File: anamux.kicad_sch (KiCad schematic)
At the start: 3 parts, among them J51 Conn_02x08_Odd_Even, U26 CD4051B

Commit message: WIP v0.2.0 changes
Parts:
- J45: renamed from J51; value Conn_02x08_Odd_Even -> Conn_01x08; footprint HL_Connector_Pad_2.54mm:Pad_2x08_P2.54_1.7x1.7_Rect-Oct -> HL_Connector_Pad_2.54mm:Pad_1x08_P2.54_1.7x1.7_Oct; symbol Connector_Generic:Conn_02x08_Odd_Even -> Connector_Generic:Conn_01x08
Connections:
- net GND: no longer J45.1 (Pin_1), J45.11 (Pin_11), J45.13 (Pin_13), J45.15 (Pin_15), J45.3 (Pin_3), J45.5 (Pin_5), J45.7 (Pin_7), J45.9 (Pin_9)
- net X0: now also J45.1 (Pin_1); no longer J45.2 (Pin_2)
- net X1: now also J45.2 (Pin_2); no longer J45.4 (Pin_4)
- net X2: now also J45.3 (Pin_3); no longer J45.6 (Pin_6)
- net X3: now also J45.4 (Pin_4); no longer J45.8 (Pin_8)
- net X4: now also J45.5 (Pin_5); no longer J45.10 (Pin_10)
- net X5: now also J45.6 (Pin_6); no longer J45.12 (Pin_12)
- net X6: now also J45.7 (Pin_7); no longer J45.14 (Pin_14)
- net X7: now also J45.8 (Pin_8); no longer J45.16 (Pin_16)

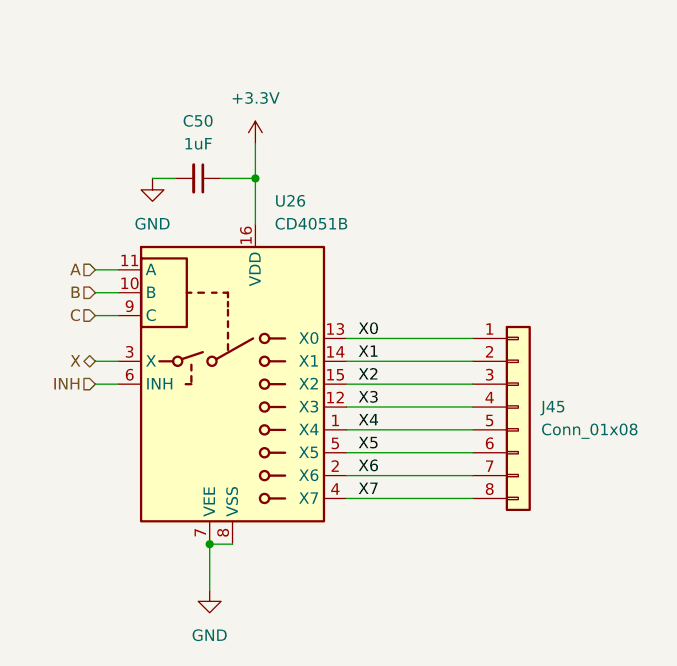
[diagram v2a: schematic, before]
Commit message: Assign part numbers and finish other 0.2.0 changes
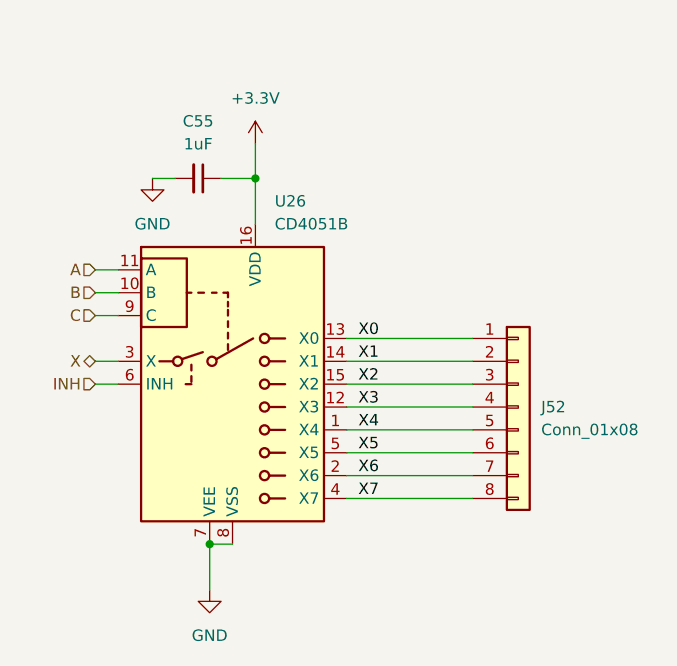
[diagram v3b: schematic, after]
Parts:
- J52: renamed from J45; LCSC (none) -> C492407
- renumbered C50 to C55
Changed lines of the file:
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@@
 		(dnp no)
 		(fields_autoplaced yes)
-		(property "Reference" "J45"
+		(property "Reference" "J52"
 			(at 123.19 78.7399 0)
 			(effects
@@
 					(size 1.27 1.27)
 				)
+			)
+		)
+		(property "LCSC" "C492407"
+			(at 120.65 78.74 0)
+			(effects
+				(font
+					(size 1.27 1.27)
+				)
+				(hide yes)
 			)
 		)
@@
 			(project ""
 				(path "/7eeba806-440e-4671-bc07-69fe183910a7/c1640104-e93c-4dad-89ee-86b02155c684/6bf2b6cc-eb81-4d9f-a81d-b7f6cfd4faa9"
-					(reference "J45")
+					(reference "J52")
 					(unit 1)
 				)
 				(path "/7eeba806-440e-4671-bc07-69fe183910a7/c1640104-e93c-4dad-89ee-86b02155c684/7f1d0812-6a9e-4744-8af9-695086760ff2"
-					(reference "J55")
+					(reference "J61")
 					(unit 1)
 				)
 				(path "/7eeba806-440e-4671-bc07-69fe183910a7/c1640104-e93c-4dad-89ee-86b02155c684/884a68a7-a98a-499d-b804-4c3e5a6711fb"
-					(reference "J49")
+					(reference "J56")
 					(unit 1)
 				)
 				(path "/7eeba806-440e-4671-bc07-69fe183910a7/c1640104-e93c-4dad-89ee-86b02155c684/93528cc8-9ea6-4e83-9001-dc55f14534f1"
-					(reference "J54")
+					(reference "J60")
 					(unit 1)
 				)
@@
 		(dnp no)
 		(fields_autoplaced yes)
-		(property "Reference" "#PWR0196"
+		(property "Reference" "#PWR0207"
 			(at 80.01 59.69 0)
 			(effects
@@
 			(project "HALSPA"
 				(path "/7eeba806-440e-4671-bc07-69fe183910a7/c1640104-e93c-4dad-89ee-86b02155c684/6bf2b6cc-eb81-4d9f-a81d-b7f6cfd4faa9"
-					(reference "#PWR0196")
+					(reference "#PWR0207")
 					(unit 1)
 				)
 				(path "/7eeba806-440e-4671-bc07-69fe183910a7/c1640104-e93c-4dad-89ee-86b02155c684/7f1d0812-6a9e-4744-8af9-695086760ff2"
-					(reference "#PWR0238")
+					(reference "#PWR0243")
 					(unit 1)
 				)
 				(path "/7eeba806-440e-4671-bc07-69fe183910a7/c1640104-e93c-4dad-89ee-86b02155c684/884a68a7-a98a-499d-b804-4c3e5a6711fb"
-					(reference "#PWR0214")
+					(reference "#PWR0223")
 					(unit 1)
 				)
 				(path "/7eeba806-440e-4671-bc07-69fe183910a7/c1640104-e93c-4dad-89ee-86b02155c684/93528cc8-9ea6-4e83-9001-dc55f14534f1"
-					(reference "#PWR0234")
+					(reference "#PWR0240")
 					(unit 1)
 				)
@@
 		(dnp no)
 		(fields_autoplaced yes)
-		(property "Reference" "#PWR0197"
+		(property "Reference" "#PWR0208"
 			(at 86.36 105.41 0)
 			(effects
@@
 			(project "HALSPA"
 				(path "/7eeba806-440e-4671-bc07-69fe183910a7/c1640104-e93c-4dad-89ee-86b02155c684/6bf2b6cc-eb81-4d9f-a81d-b7f6cfd4faa9"
-					(reference "#PWR0197")
+					(reference "#PWR0208")
 					(unit 1)
 				)
 				(path "/7eeba806-440e-4671-bc07-69fe183910a7/c1640104-e93c-4dad-89ee-86b02155c684/7f1d0812-6a9e-4744-8af9-695086760ff2"
-					(reference "#PWR0239")
+					(reference "#PWR0244")
 					(unit 1)
 				)
 				(path "/7eeba806-440e-4671-bc07-69fe183910a7/c1640104-e93c-4dad-89ee-86b02155c684/884a68a7-a98a-499d-b804-4c3e5a6711fb"
-					(reference "#PWR0215")
+					(reference "#PWR0224")
 					(unit 1)
 				)
 				(path "/7eeba806-440e-4671-bc07-69fe183910a7/c1640104-e93c-4dad-89ee-86b02155c684/93528cc8-9ea6-4e83-9001-dc55f14534f1"
-					(reference "#PWR0235")
+					(reference "#PWR0241")
 					(unit 1)
 				)
@@
 		(dnp no)
 		(fields_autoplaced yes)
-		(property "Reference" "C50"
+		(property "Reference" "C55"
 			(at 85.0836 46.99 90)
 			(effects
@@
 			(project "HALSPA"
 				(path "/7eeba806-440e-4671-bc07-69fe183910a7/c1640104-e93c-4dad-89ee-86b02155c684/6bf2b6cc-eb81-4d9f-a81d-b7f6cfd4faa9"
-					(reference "C50")
+					(reference "C55")
 					(unit 1)
 				)
 				(path "/7eeba806-440e-4671-bc07-69fe183910a7/c1640104-e93c-4dad-89ee-86b02155c684/7f1d0812-6a9e-4744-8af9-695086760ff2"
-					(reference "C60")
+					(reference "C65")
 					(unit 1)
 				)
 				(path "/7eeba806-440e-4671-bc07-69fe183910a7/c1640104-e93c-4dad-89ee-86b02155c684/884a68a7-a98a-499d-b804-4c3e5a6711fb"
-					(reference "C54")
+					(reference "C59")
 					(unit 1)
 				)
 				(path "/7eeba806-440e-4671-bc07-69fe183910a7/c1640104-e93c-4dad-89ee-86b02155c684/93528cc8-9ea6-4e83-9001-dc55f14534f1"
-					(reference "C59")
+					(reference "C64")
 					(unit 1)
 				)
@@
 		(dnp no)
 		(fields_autoplaced yes)
-		(property "Reference" "#PWR0198"
+		(property "Reference" "#PWR0209"
 			(at 91.44 53.34 0)
 			(effects
@@
 			(project "HALSPA"
 				(path "/7eeba806-440e-4671-bc07-69fe183910a7/c1640104-e93c-4dad-89ee-86b02155c684/6bf2b6cc-eb81-4d9f-a81d-b7f6cfd4faa9"
-					(reference "#PWR0198")
+					(reference "#PWR0209")
 					(unit 1)
 				)
 				(path "/7eeba806-440e-4671-bc07-69fe183910a7/c1640104-e93c-4dad-89ee-86b02155c684/7f1d0812-6a9e-4744-8af9-695086760ff2"
-					(reference "#PWR0240")
+					(reference "#PWR0245")
 					(unit 1)
 				)
 				(path "/7eeba806-440e-4671-bc07-69fe183910a7/c1640104-e93c-4dad-89ee-86b02155c684/884a68a7-a98a-499d-b804-4c3e5a6711fb"
-					(reference "#PWR0216")
+					(reference "#PWR0225")
 					(unit 1)
 				)
 				(path "/7eeba806-440e-4671-bc07-69fe183910a7/c1640104-e93c-4dad-89ee-86b02155c684/93528cc8-9ea6-4e83-9001-dc55f14534f1"
-					(reference "#PWR0236")
-					(unit 1)
-				)
+					(reference "#PWR0242")
+					(unit 1)
+				)

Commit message: Update the title blocks
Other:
- company: (none) -> Hat Labs Oy
- title: (none) -> HALSPA - Hat Labs Spaghetti Board
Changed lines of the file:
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@@
 	(generator_version "9.0")
 	(paper "A4")
+	(title_block
+		(title "HALSPA - Hat Labs Spaghetti Board")
+		(date "2025-04-17")
+		(rev "v0.2.0")
+		(company "Hat Labs Oy")
+		(comment 1 "See the accompanying LICENSE.md file for license details.")
+	)
 	(junction
 		(at 91.44 53.34)

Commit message: Fix minor production issues
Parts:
- J52: JLCPCB_CORRECTION (none) -> 0;8.89;270
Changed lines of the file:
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@@
+			)
+		)
+		(property "JLCPCB_CORRECTION" "0;8.89;270"
+			(at 120.65 78.74 0)
+			(effects
+				(font
+					(size 1.27 1.27)
+				)
 			)
 		)

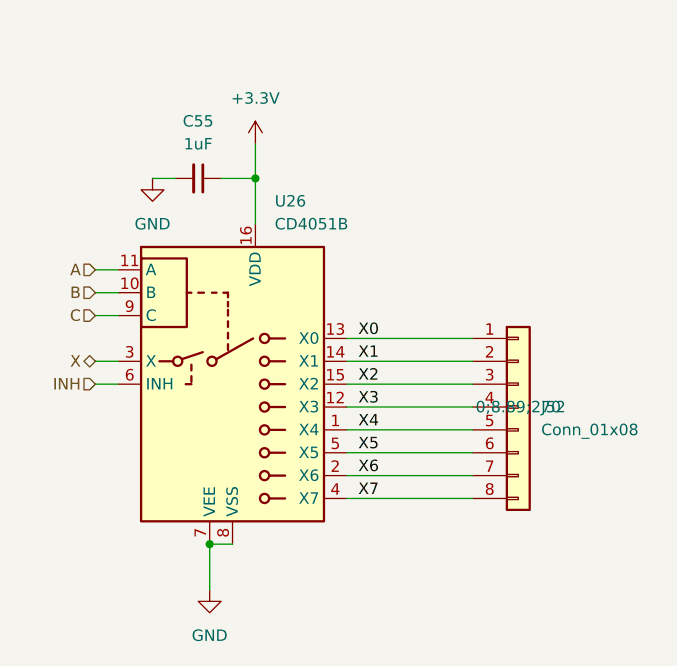
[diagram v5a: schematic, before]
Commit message: Improve MCU2 layout; document curlim12v CSA
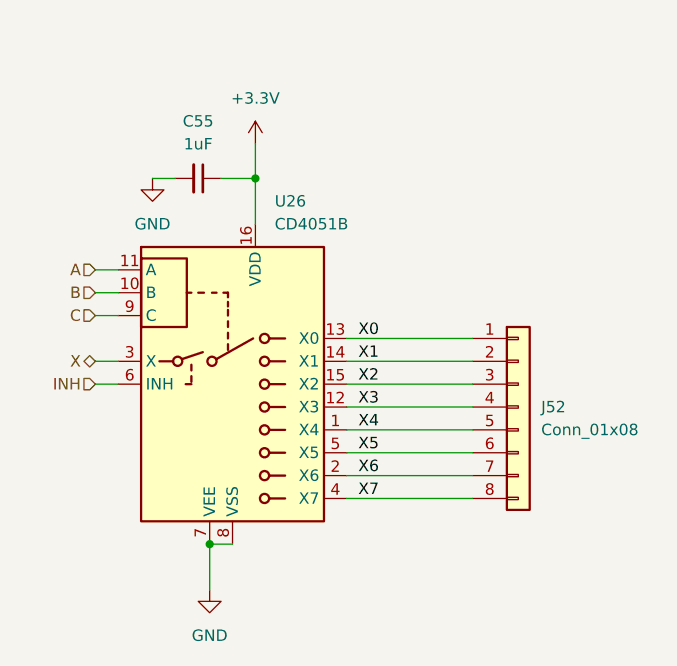
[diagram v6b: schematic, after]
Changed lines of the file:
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@@
 					(size 1.27 1.27)
 				)
+				(hide yes)
 			)
 		)
@@
 				)
 				(path "/7eeba806-440e-4671-bc07-69fe183910a7/c1640104-e93c-4dad-89ee-86b02155c684/7f1d0812-6a9e-4744-8af9-695086760ff2"
-					(reference "#PWR0243")
+					(reference "#PWR0244")
 					(unit 1)
 				)
@@
 				)
 				(path "/7eeba806-440e-4671-bc07-69fe183910a7/c1640104-e93c-4dad-89ee-86b02155c684/93528cc8-9ea6-4e83-9001-dc55f14534f1"
-					(reference "#PWR0240")
+					(reference "#PWR0241")
 					(unit 1)
 				)
@@
 				)
 				(path "/7eeba806-440e-4671-bc07-69fe183910a7/c1640104-e93c-4dad-89ee-86b02155c684/7f1d0812-6a9e-4744-8af9-695086760ff2"
-					(reference "#PWR0244")
+					(reference "#PWR0245")
 					(unit 1)
 				)
@@
 				)
 				(path "/7eeba806-440e-4671-bc07-69fe183910a7/c1640104-e93c-4dad-89ee-86b02155c684/93528cc8-9ea6-4e83-9001-dc55f14534f1"
-					(reference "#PWR0241")
+					(reference "#PWR0242")
 					(unit 1)
 				)
@@
 				)
 				(path "/7eeba806-440e-4671-bc07-69fe183910a7/c1640104-e93c-4dad-89ee-86b02155c684/7f1d0812-6a9e-4744-8af9-695086760ff2"
-					(reference "#PWR0245")
+					(reference "#PWR0246")
 					(unit 1)
 				)
@@
 				)
 				(path "/7eeba806-440e-4671-bc07-69fe183910a7/c1640104-e93c-4dad-89ee-86b02155c684/93528cc8-9ea6-4e83-9001-dc55f14534f1"
-					(reference "#PWR0242")
-					(unit 1)
-				)
+					(reference "#PWR0243")
+					(unit 1)
+				)

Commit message: Update anamux labeling and title blocks
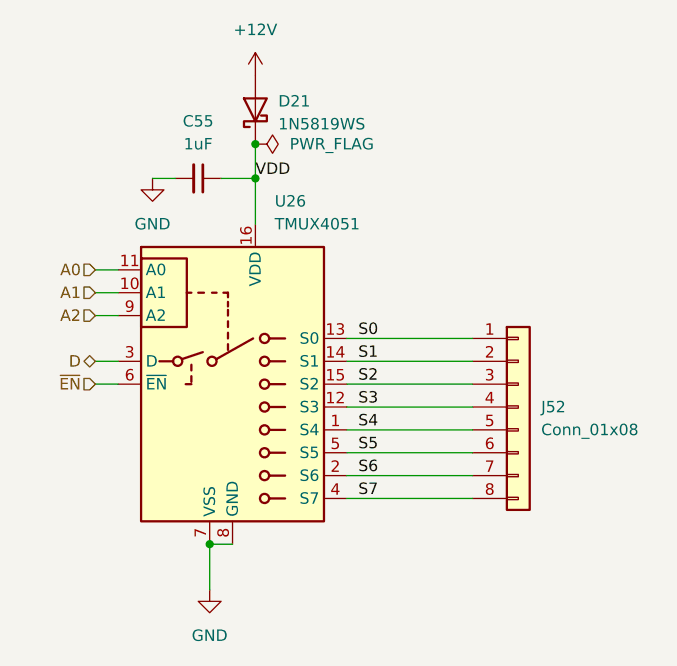
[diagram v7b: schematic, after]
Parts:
- added D21: 1N5819WS, Diode_SMD:D_SOD-323, symbol Diode:1N5819WS
- U26: value CD4051B -> TMUX4051; footprint Package_SO:SOIC-16_3.9x9.9mm_P1.27mm -> Package_SO:TSSOP-16_4.4x5mm_P0.65mm; symbol Analog_Switch:CD4051B -> HL_Analog_Switch:TMUX4051; LCSC C21379 -> C5449352
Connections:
- net +3.3V renamed VDD
- net VDD: now also D21.1 (K)
- net A renamed A0
- net B renamed A1
- net C renamed A2
- net INH renamed ~{EN}
- net X renamed D
- net X0 renamed S0
- net X1 renamed S1
- net X2 renamed S2
- net X3 renamed S3
- net X4 renamed S4
- net X5 renamed S5
- net X6 renamed S6
- net X7 renamed S7
- new net +12V: D21.2 (A)

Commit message: Adjust trimmer test pads
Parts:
- D21: LCSC (none) -> C191023
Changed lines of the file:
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@@
+			)
+		)
+		(property "LCSC" "C191023"
+			(at 91.44 45.72 90)
+			(effects
+				(font
+					(size 1.27 1.27)
+				)
+				(hide yes)
 			)
 		)
